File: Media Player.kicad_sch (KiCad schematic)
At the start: 35 parts, among them J1 PH2.0, J2 MEM2075-00-140-01-A, J3 USB_C_Receptacle_USB2.0_14P, SW1 SW_Push, SW2 SW_Push, SW3 SW_Push, SW4 SW_Push, SW5 SW_Push, SW6 SW_Push, SW7 SW_SPST, U1 ESP32-S3-WROOM-1

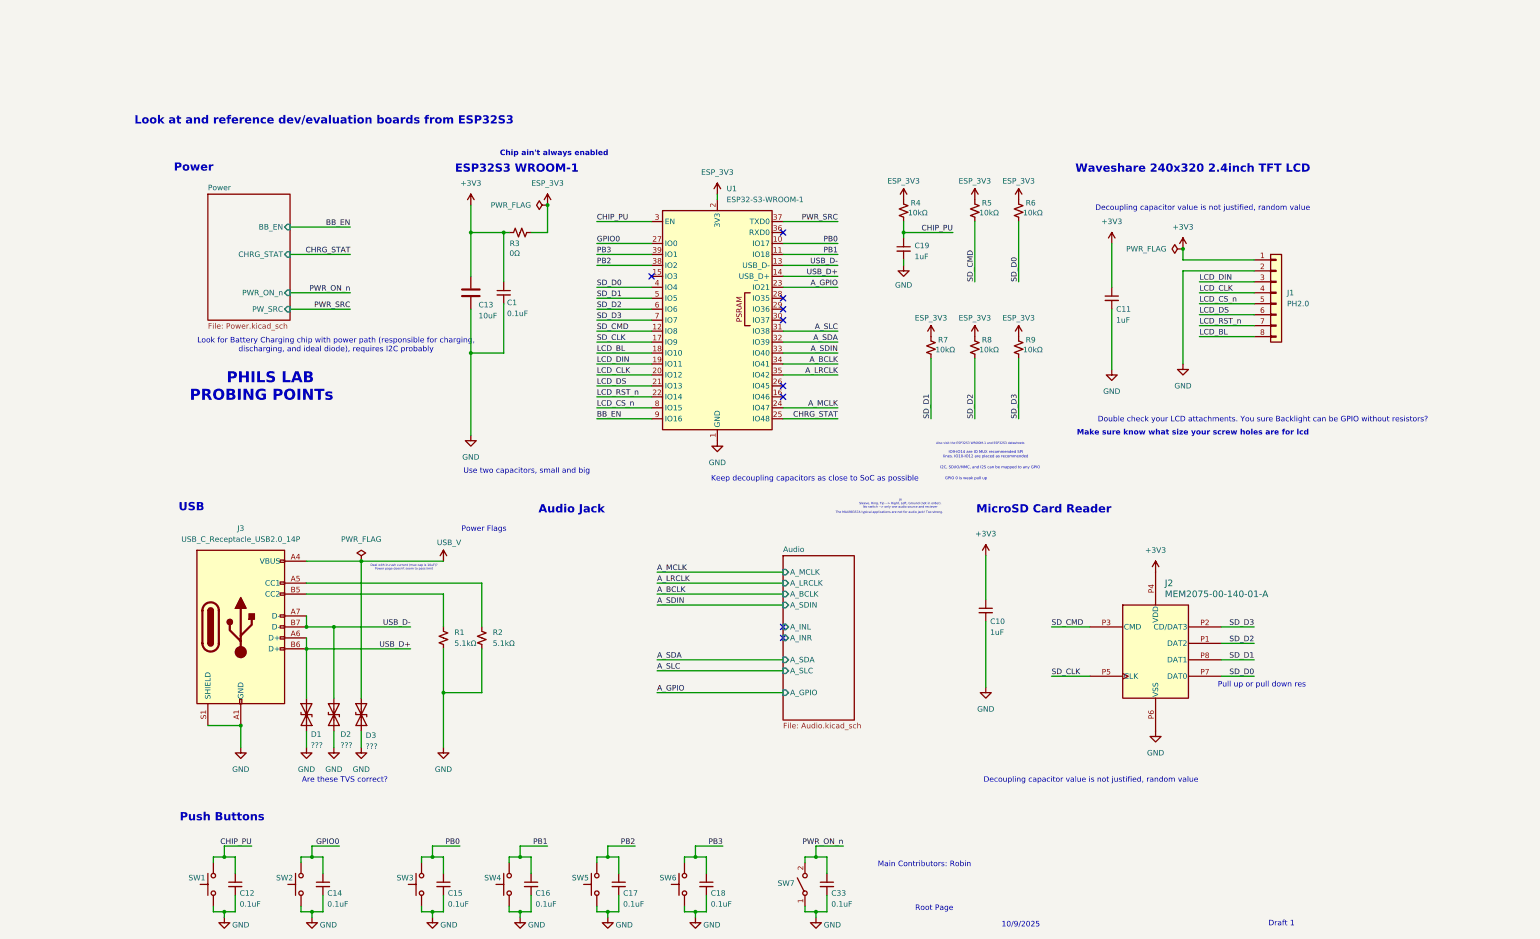
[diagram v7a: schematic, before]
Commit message: Draft 2: Protection circuitry and fixed I/O signals
Still missing PMOS spec for reverse polarity battery protection. Added TVS to USB, voltage divided certain output signals from ICs into ESP GPIO. Checked some component values.
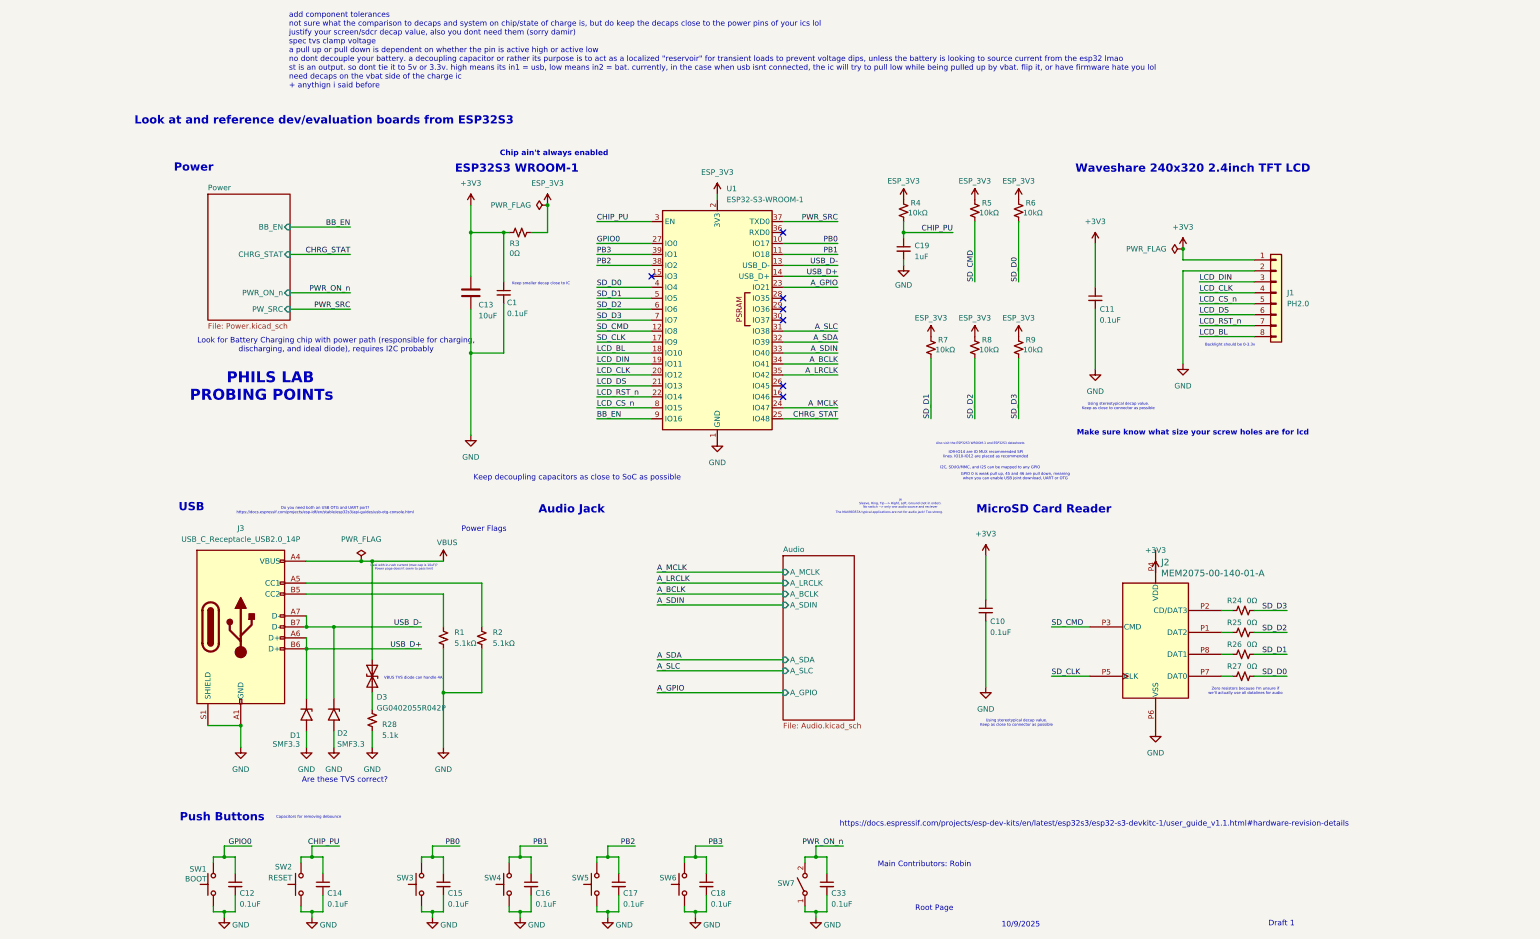
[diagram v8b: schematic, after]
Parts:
- removed D1: ???, Diode_THT:D_DO-201AE_P15.24mm_Horizontal, symbol Diode:1.5KExxCA
- added D1: SMF3.3, Diode_SMD:D_SMF, symbol Diode:SMF33A
- added R24, R25, R26, R27: 0Ω, symbol Device:R_Small_US
- added R28: 5.1k, symbol Device:R_Small_US
- C10, C11: value 1uF -> 0.1uF
- D2: value ??? -> SMF3.3; footprint Diode_THT:D_DO-201AE_P15.24mm_Horizontal -> Diode_SMD:D_SMF; symbol Diode:1.5KExxCA -> Diode:SMF33A
- D3: value ??? -> GG0402055R042P
- SW1: value SW_Push -> BOOT
- SW2: value SW_Push -> RESET
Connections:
- net +3V3: no longer J2.P4 (VDD)
- net CHIP_PU: now also C14.1, SW2.2; no longer C12.1, SW1.2
- net GND: now also D2.2 (A2), D1.2 (A2), R28.2; no longer D2.1 (A1), D3.1 (A1)
- net GPIO0: now also C12.1, SW1.2; no longer C14.1, SW2.2
- net SD_D0: now also R27.2; no longer J2.P7 (DAT0)
- net SD_D1: now also R26.2; no longer J2.P8 (DAT1)
- net SD_D2: now also R25.2; no longer J2.P1 (DAT2)
- net SD_D3: now also R24.2; no longer J2.P2 (CD/DAT3)
- net USB_D+: now also D1.1 (A1)
- net USB_D-: now also D2.1 (A1); no longer D2.2 (A2)
- net USB_V renamed VBUS
- new net: J2.P1 (DAT2), R25.1
- new net: D3.1 (A1), R28.1
- new net: J2.P7 (DAT0), R27.1
- new net: J2.P2 (CD/DAT3), R24.1
- new net: J2.P8 (DAT1), R26.1
- no-connect marks 9 -> 7
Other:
- sheet Audio ports: added none; removed A_INL, A_INR
- note added: "Backlight should be 0-3.3v"
- note added: "Capacitors for removing debounce"
- note added: "Do you need both an USB OTG and UART port? https://docs.espressif.com/projects/esp-idf/en/stable/esp32s3/api-guides/usb-otg-console.html"
- note added: "GPIO 0 is weak pull up, 45 and 46 are pull down, meaning when you can enable USB joint download, UART or OTG"
- note added: "Keep smaller decap close to IC"
- note added: "Using stereotypical decap value. Keep as close to connector as possible"
- note added: "VBUS TVS diode can handle 4A."
- note added: "Zero resistors because I'm unsure if we'll actually use all datalines for audio"
- note added: "add component tolerances not sure what the comparison to decaps and system on chip/state of charge is, but do keep the decaps close to the power pins of your ics lol justify your screen/sdcr decap value, also you dont need them (sorry damir) spec tvs clamp voltage a pull up or pull down is dependent on whether the pin is active high or active low no dont decouple your battery. a decoupling capaci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"
- note added: "https://docs.espressif.com/projects/esp-dev-kits/en/latest/esp32s3/esp32-s3-devkitc-1/user_guide_v1.1.html#hardware-revision-details"
- note removed: "Decoupling capacitor value is not justified, random value"
- note removed: "Double check your LCD attachments. You sure Backlight can be GPIO without resistors?"
- note removed: "GPIO 0 is weak pull up"
- note removed: "Pull up or pull down res"
- note removed: "Use two capacitors, small and big"
- moved on the sheet: C11, D3, J2
